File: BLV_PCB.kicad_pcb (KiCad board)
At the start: 4 copper layers, 90 x 90 mm, 92 parts, among them J1 Cube0_UART_JST-PH, J10 USB_C_USB2.0_16P, J11 Micro_SD_Card, J12 RF SMA, J2 Cube0_UART_JST-PH, J3 Cube0_UART_JST-PH, J4 Cube0_UART_Debug, J5 Cube0_UART_Debug, J6 Cube0_UART_Debug, J7 Dupont Debug Headers, J8 USB_C_USB2.0_16P, J9 RF SMA, Q1 Si2301CDS, Q2 Si2301CDS, SW1 SW_Push, SW2 SW_RUN, SW3 SW_Push, U1 W25Q128JVS, U2 RP2350_60QFN, U3 AMS1117-3.3, U4 TPS61230DRCR, U5 E32-400M30S, U6 NEO-M9N, Y1 ABM8_262_T3

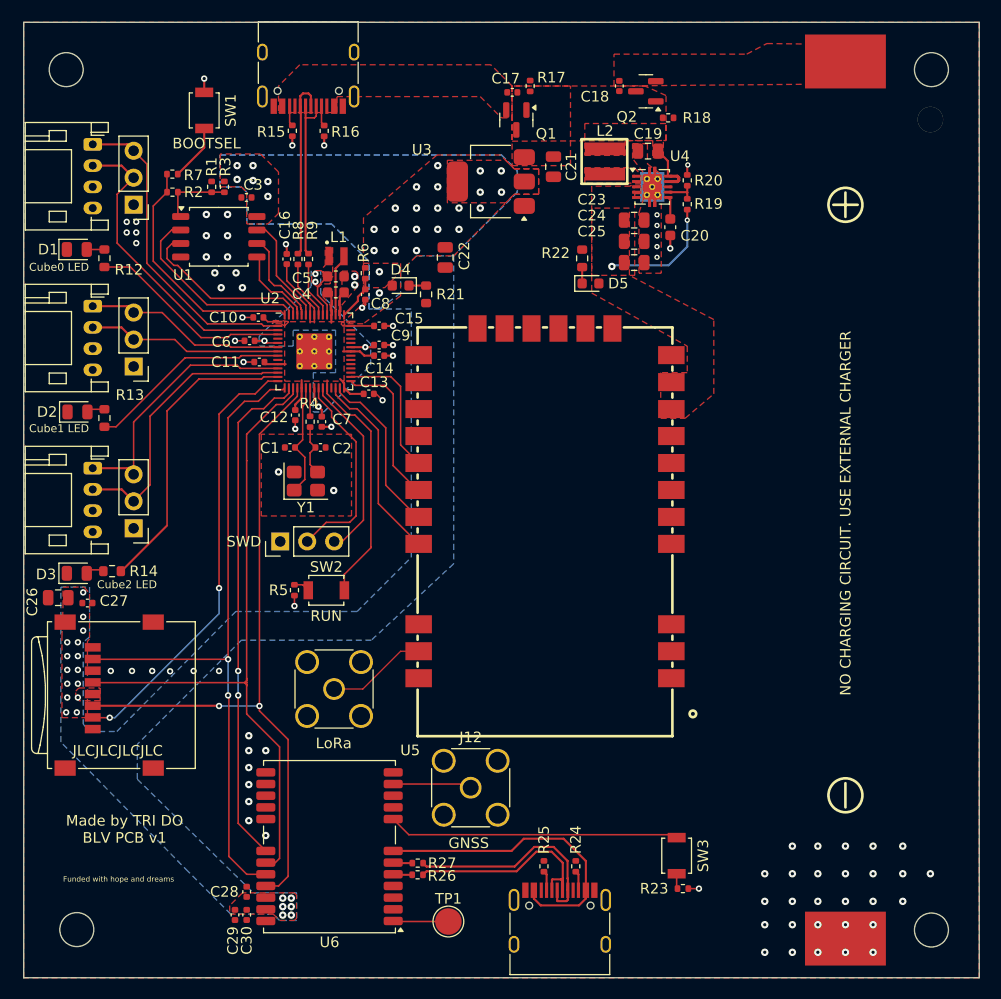
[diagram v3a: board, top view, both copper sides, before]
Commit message: Updated EBYTE placement
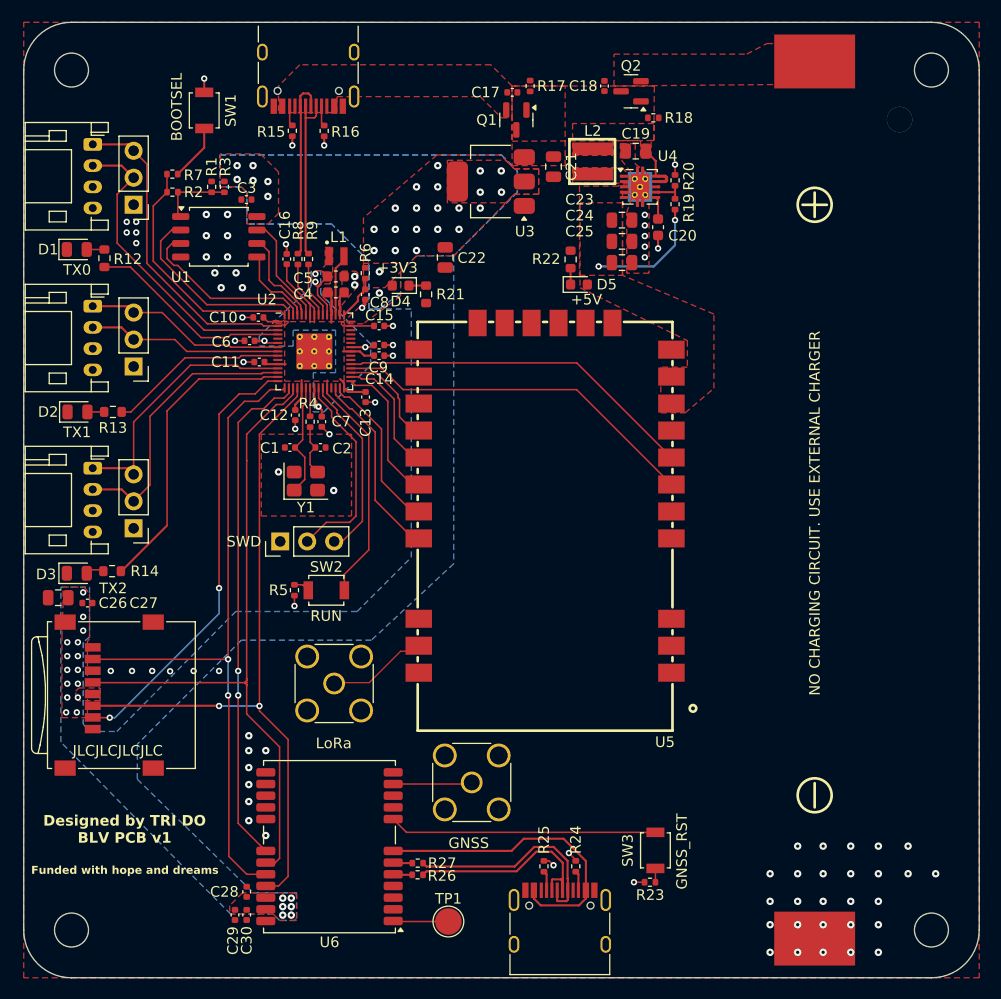
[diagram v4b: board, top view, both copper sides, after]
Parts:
- moved R23 3.16 mm to (189.0, 121.0), turned to 0 degrees
- moved BAT1 2.90 mm to (204.5, 85.0)
- moved SW3 2.06 mm to (189.5, 118.0)
- moved C18 1.40 mm to (184.7, 46.0)
- moved Q2 1.40 mm to (187.2, 46.5)
- moved R18 1.40 mm to (189.3, 49.0)
- moved C19 1.15 mm to (187.7, 52.1)
- moved C20 1.15 mm to (189.8, 59.3)
- moved C23 1.15 mm to (186.3, 58.6)
- moved C24 1.15 mm to (186.3, 60.6)
- moved C25 1.15 mm to (186.3, 62.6)
- moved L2 1.15 mm to (183.6, 53.1)
- moved R19 1.15 mm to (191.3, 57.1)
- moved R20 1.15 mm to (191.3, 54.9)
- moved U4 1.15 mm to (188.1, 55.5)
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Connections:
- U2 pad 33: unconnected-(U2-GPIO21-Pad33) -> /MCU/RF_RST
- U2 pad 34: unconnected-(U2-GPIO22-Pad34) -> /MCU/RF_RXEN
- U2 pad 35: unconnected-(U2-GPIO23-Pad35) -> /MCU/RF_TXEN
- U2 pad 36: /MCU/BUS_I2C0_SDA -> unconnected-(U2-GPIO24-Pad36)
- U2 pad 37: /MCU/BUS_I2C0_SCL -> unconnected-(U2-GPIO25-Pad37)
- U5 pad 21: /RF/NRST -> /MCU/RF_RST
- U5 pad 6: unconnected-(U5-RXEN-Pad6) -> /MCU/RF_RXEN
- U5 pad 7: unconnected-(U5-TXEN-Pad7) -> /MCU/RF_TXEN
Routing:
- net /MCU/RF_RXEN: track 0.00 -> 34.7 mm
- net /MCU/RF_TXEN: track 0.00 -> 33.9 mm
- net /MCU/RF_RST: track 0.00 -> 10.0 mm
- net /MCU/Cube1_LED: track 19.1 -> 16.9 mm
- net GND: track 20.0 -> 22.1 mm, vias 84 -> 85
- net /GNSS & MicroSD/GNSS_RST: track 27.4 -> 26.3 mm
- net /MCU/RF_SPI_MISO: track 13.0 -> 11.9 mm
- net /RF/RF_ANT: track 9.44 -> 8.60 mm
- net /MCU/RF_SPI_MOSI: track 14.6 -> 13.9 mm
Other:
- outline, holes or cut-outs redrawn
- rule pad_to_mask_clearance: 0 -> 0.1
- board text added: "+3V3"
- board text added: "+5V"
- board text added: "Designed by TRI DO BLV PCB v1"
- board text added: "GNSS_RST"
- board text added: "TX0"
- board text added: "TX1"
- board text added: "TX2"
- board text removed: "Cube0 LED"
- board text removed: "Cube1 LED"
- board text removed: "Cube2 LED"
- board text removed: "Made by TRI DO BLV PCB v1"

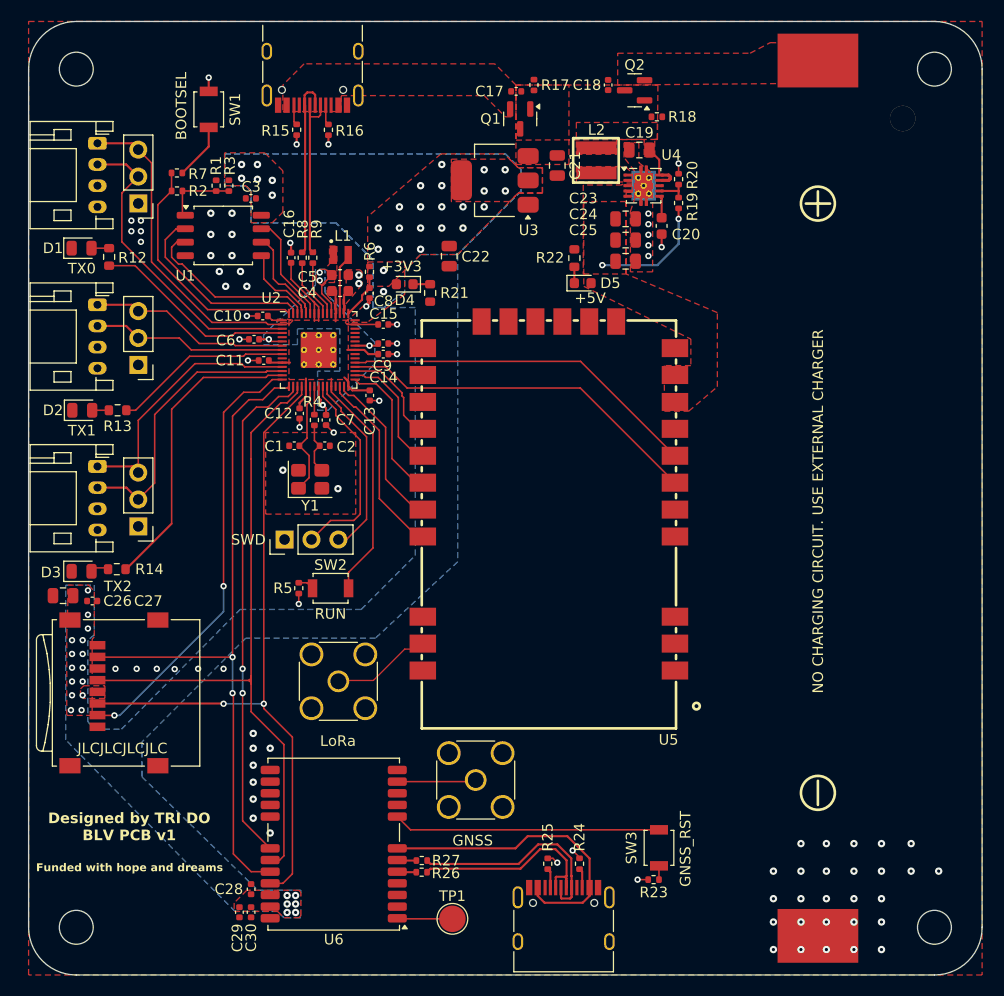
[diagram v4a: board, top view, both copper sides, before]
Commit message: Add Buck-Boost 3V3 power
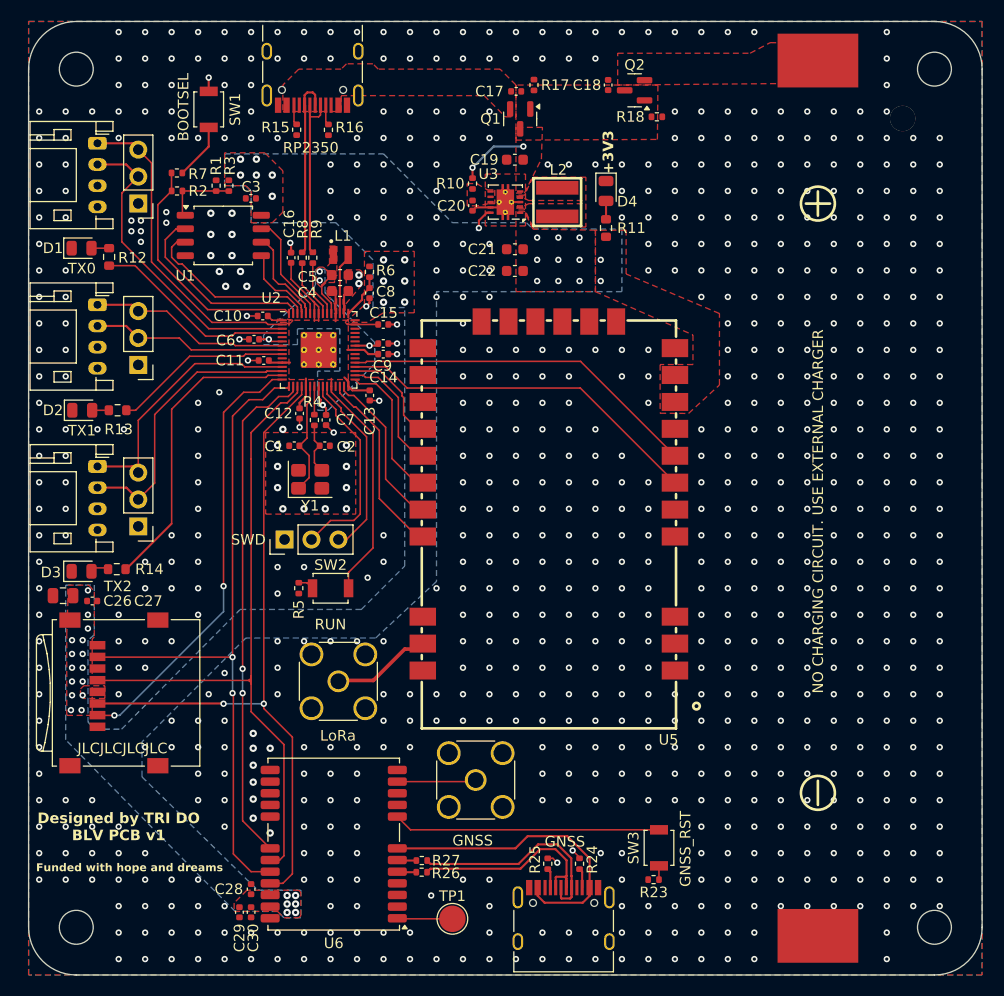
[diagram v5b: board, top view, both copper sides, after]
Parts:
- removed C23, C24, C25: 22u, Capacitor_SMD:C_0805_2012Metric
- removed D5: GREEN, LED_SMD:LED_0603_1608Metric
- removed R19: 200k, Resistor_SMD:R_0402_1005Metric
- removed R20: 49k9, Resistor_SMD:R_0402_1005Metric
- removed R21, R22: 2k2, Resistor_SMD:R_0603_1608Metric
- removed U4: TPS61230DRCR, Package_SON:Texas_S-PVSON-N10_ThermalVias
- added R10: 100, Resistor_SMD:R_0402_1005Metric, F.Cu at (171.9, 55.3)
- added R11: 1k, Resistor_SMD:R_0603_1608Metric, F.Cu at (184.5, 59.5)
- C19: value 22u -> 10u; footprint Capacitor_SMD:C_0805_2012Metric -> Capacitor_SMD:C_0603_1608Metric
- C20: value 10u -> 100n; footprint Capacitor_SMD:C_0603_1608Metric -> Capacitor_SMD:C_0402_1005Metric
- C21, C22: footprint Capacitor_SMD:C_0805_2012Metric -> Capacitor_SMD:C_0603_1608Metric
- D4: value YELLOW -> GREEN; footprint LED_SMD:LED_0603_1608Metric -> LED_SMD:LED_0805_2012Metric
- L2: value 1u -> 2u2; footprint easyeda2kicad:IND-SMD_L4.0-W4.0_XFL4020-102MEB -> easyeda2kicad:IND-SMD_L4.0-W4.0_VLS4012ET
- U3: value AMS1117-3.3 -> TPS63001DRCR; footprint Package_TO_SOT_SMD:SOT-223-3_TabPin2 -> Package_SON:Texas_DRC0010J_ThermalVias
- moved D4 20.9 mm to (184.5, 56.0), turned to -90 degrees
- moved C20 18.0 mm to (171.9, 57.4)
- moved C19 11.8 mm to (175.9, 53.0)
- moved C21 8.85 mm to (175.9, 61.5), turned to 180 degrees
- moved C22 6.36 mm to (175.9, 63.5), turned to 180 degrees
- moved L2 5.40 mm to (179.9, 57.0)
- moved U3 2.28 mm to (175.0, 57.0)
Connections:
- C20 pad 1: /Power/5V_SMPS_SS -> /Power/3V3_EN
- C21 pad 1: /Power/Vin -> +3V3
- D4 pad 1: /Power/LED_3V3 -> GND
- D4 pad 2: +3V3 -> /Power/3V3_LED
- L2 pad 1: /Power/Vin -> /Power/L1
- L2 pad 2: /Power/5V_SMPS_SW -> /Power/L2
- U3 pad 1: GND -> +3V3
- U3 pad 2: +3V3 -> /Power/L2
- U3 pad 3: /Power/Vin -> GND
- U5 pad 10: +5V -> +3V3
- U5 pad 9: +5V -> +3V3
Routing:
- net +5V: track 11.7 -> 0.00 mm, vias 2 -> 0
- net /Power/5V_SMPS_SS: track 2.58 -> 0.00 mm
- net /Power/5V_SMPS_FB: track 2.55 -> 0.00 mm
- net +3V3: track 49.5 -> 51.9 mm, vias 49 -> 45
- net /Power/Vin: track 4.58 -> 6.65 mm, vias 0 -> 2
- net /Power/3V3_LED: track 0.00 -> 1.74 mm
- net /Power/LED_3V3: track 1.61 -> 0.00 mm
- net /Power/LED_5V: track 1.44 -> 0.00 mm
- net GND: track 22.1 -> 21.0 mm, vias 85 -> 812
- added copper zone on F.Cu, net /Power/3V3_EN
- added copper zone on F.Cu, net /Power/L1
- added copper zone on F.Cu, net /Power/L2
- added copper zone on B.Cu, net GND
- removed copper zone on F.Cu, net +5V
- removed copper zone on F.Cu, net /Power/5V_SMPS_SW
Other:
- board text added: "RP2350"
- board text added: "We can't even afford Double-Sided PCBA"
- board text removed: "+5V"

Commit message: Added silkscreens label description and fixed DRC
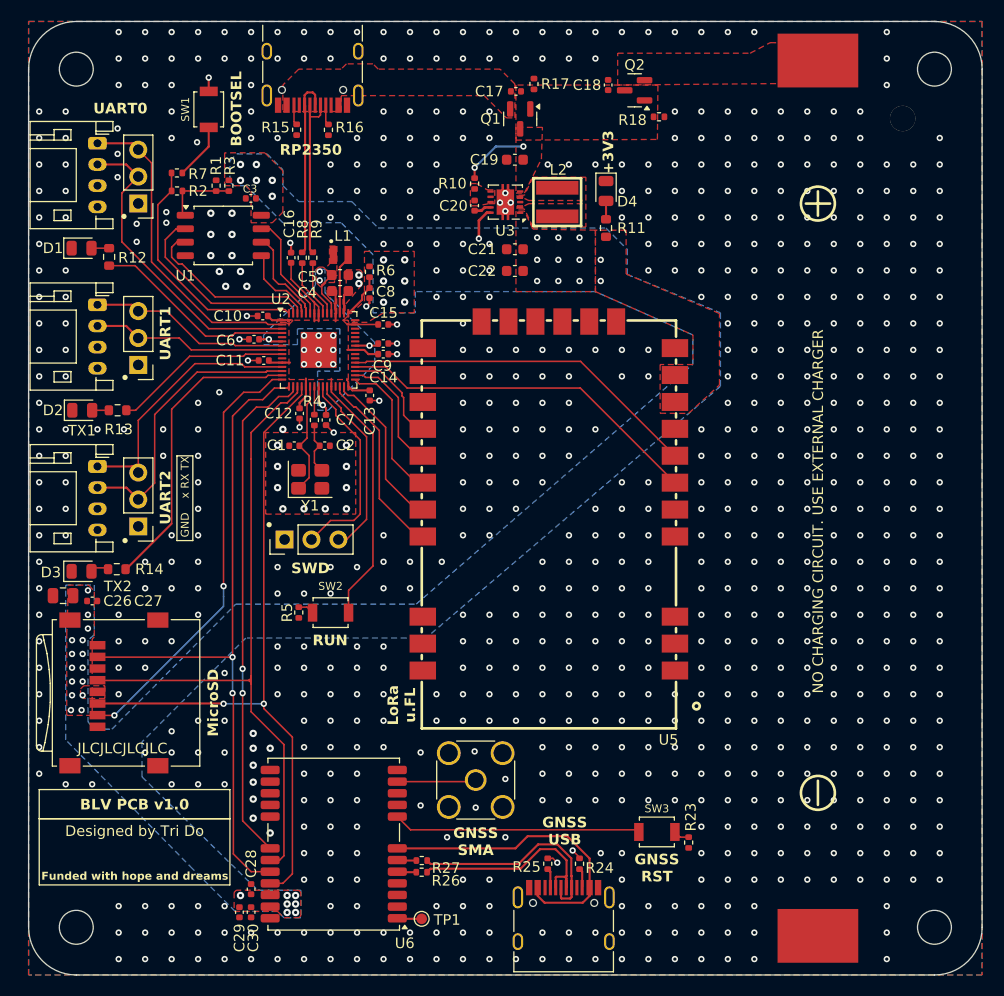
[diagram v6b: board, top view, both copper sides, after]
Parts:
- removed J9: RF SMA, Connector_Coaxial:SMA_Amphenol_132134_Vertical
- TP1: footprint TestPoint:TestPoint_Pad_D2.5mm -> TestPoint:TestPoint_Pad_D1.0mm
- U2: footprint RP2350_60QFN_minimal:RP2350-QFN-60-1EP_7x7_P0.4mm_EP3.4x3.4mm_ThermalVias -> Package_DFN_QFN:QFN-60-1EP_7x7mm_P0.4mm_EP3.4x3.4mm
- U3: footprint Package_SON:Texas_DRC0010J_ThermalVias -> Package_SON:Texas_DRC0010J
- moved R23 4.82 mm to (192.3, 117.5), turned to 90 degrees
- moved TP1 2.90 mm to (167.1, 124.7)
- moved R5 2.30 mm to (155.5, 95.8)
- moved SW2 2.30 mm to (158.5, 95.8)
- moved SW3 1.51 mm to (189.3, 116.5), turned to 180 degrees
- moved C20 0.20 mm to (172.1, 57.4)
- moved R10 0.20 mm to (172.1, 55.3)
- moved R18 0.20 mm to (189.5, 49.0)
- moved R17 0.10 mm to (177.7, 45.9)
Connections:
- U5 pad 27: /RF/RF_ANT -> unconnected-(U5-ANT-Pad27)
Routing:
- net /RF/RF_ANT: track 8.60 -> 0.00 mm
- net +3V3: track 51.9 -> 55.4 mm, vias 45 -> 46
- net GND: track 21.0 -> 17.8 mm, vias 812 -> 799
- net /GNSS & MicroSD/GNSS_RST: track 26.3 -> 23.4 mm
- net Net-(U6-~{SAFEBOOT}): track 5.22 -> 2.32 mm
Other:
- board text added: "BLV PCB v1.0"
- board text added: "Designed by Tri Do"
- board text added: "GND x RX TX"
- board text added: "GNSS RST"
- board text added: "GNSS SMA"
- board text added: "GNSS USB"
- board text added: "LoRa u.FL"
- board text added: "MicroSD"
- board text added: "UART0"
- board text added: "UART1"
- board text added: "UART2"
- board text removed: "Designed by TRI DO BLV PCB v1"
- board text removed: "GNSS"
- board text removed: "GNSS_RST"
- board text removed: "LoRa"
- board text removed: "TX0"

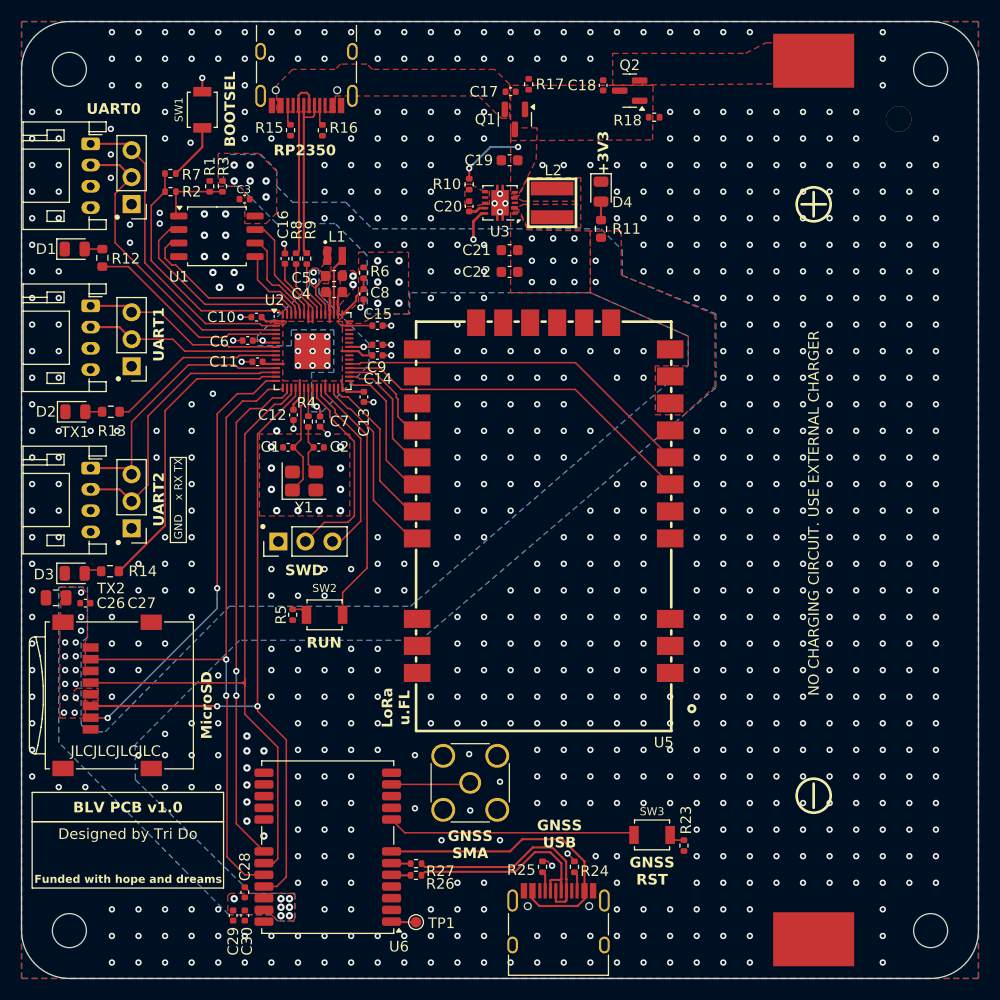
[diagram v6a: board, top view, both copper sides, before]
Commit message: Added 3D models and LCSC part numbers
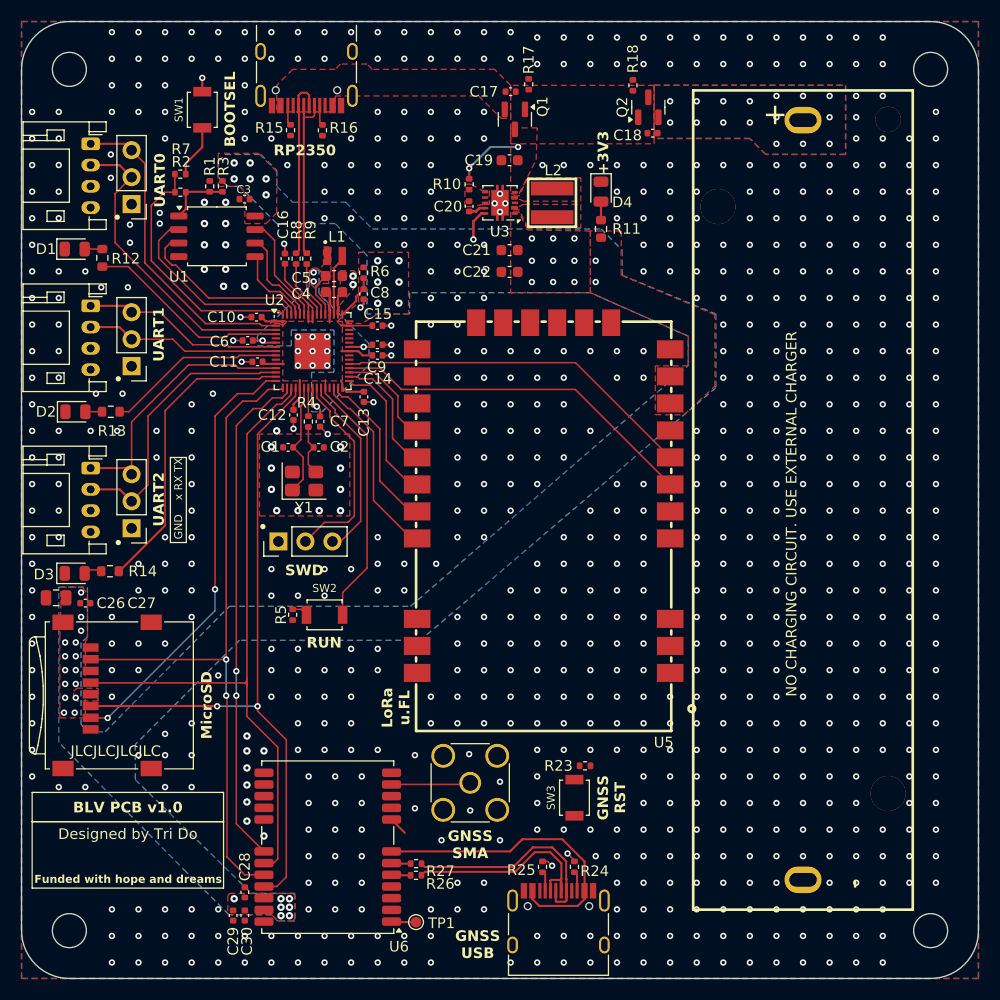
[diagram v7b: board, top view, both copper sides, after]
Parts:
- removed BAT1: BH-18650-B6AA002, easyeda2kicad:BATTERY-SMD_18650-1S-L77.1-W20.7-1
- added U4: BH-18650-A6AJ012, easyeda2kicad:BAT-TH_BH-18650-A6AJ012, F.Cu at (203.5, 85.0)
- moved R23 11.9 mm to (183.0, 110.0), turned to 180 degrees
- moved SW3 8.10 mm to (182.0, 113.0), turned to -90 degrees
- moved C18 6.47 mm to (189.3, 50.5), turned to 180 degrees
- moved R18 3.61 mm to (187.5, 46.0), turned to 90 degrees
- moved Q2 2.35 mm to (188.9, 48.1), turned to 90 degrees
- moved R2 0.93 mm to (144.9, 56.1)
- moved R7 0.93 mm to (144.9, 54.4)
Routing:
- net /GNSS & MicroSD/GNSS_RST: track 23.4 -> 1.77 mm
- net /GNSS & MicroSD/GNSS_RST_R: track 1.50 -> 0.00 mm
- net /MCU/QSPI_SS: track 23.2 -> 24.1 mm
- net GND: vias 799 -> 813
- net +BATT: vias 0 -> 16
- added copper zone on B.Cu, net +BATT
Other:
- board text removed: "TX1"
- board text removed: "TX2"
